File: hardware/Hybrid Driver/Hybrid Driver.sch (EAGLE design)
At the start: 35 parts, among them CN1 MTA100-6, CN2 SE14, U1 M57962L, U2 VLA106-15242, U3 M57962L, U4 VLA106-15242

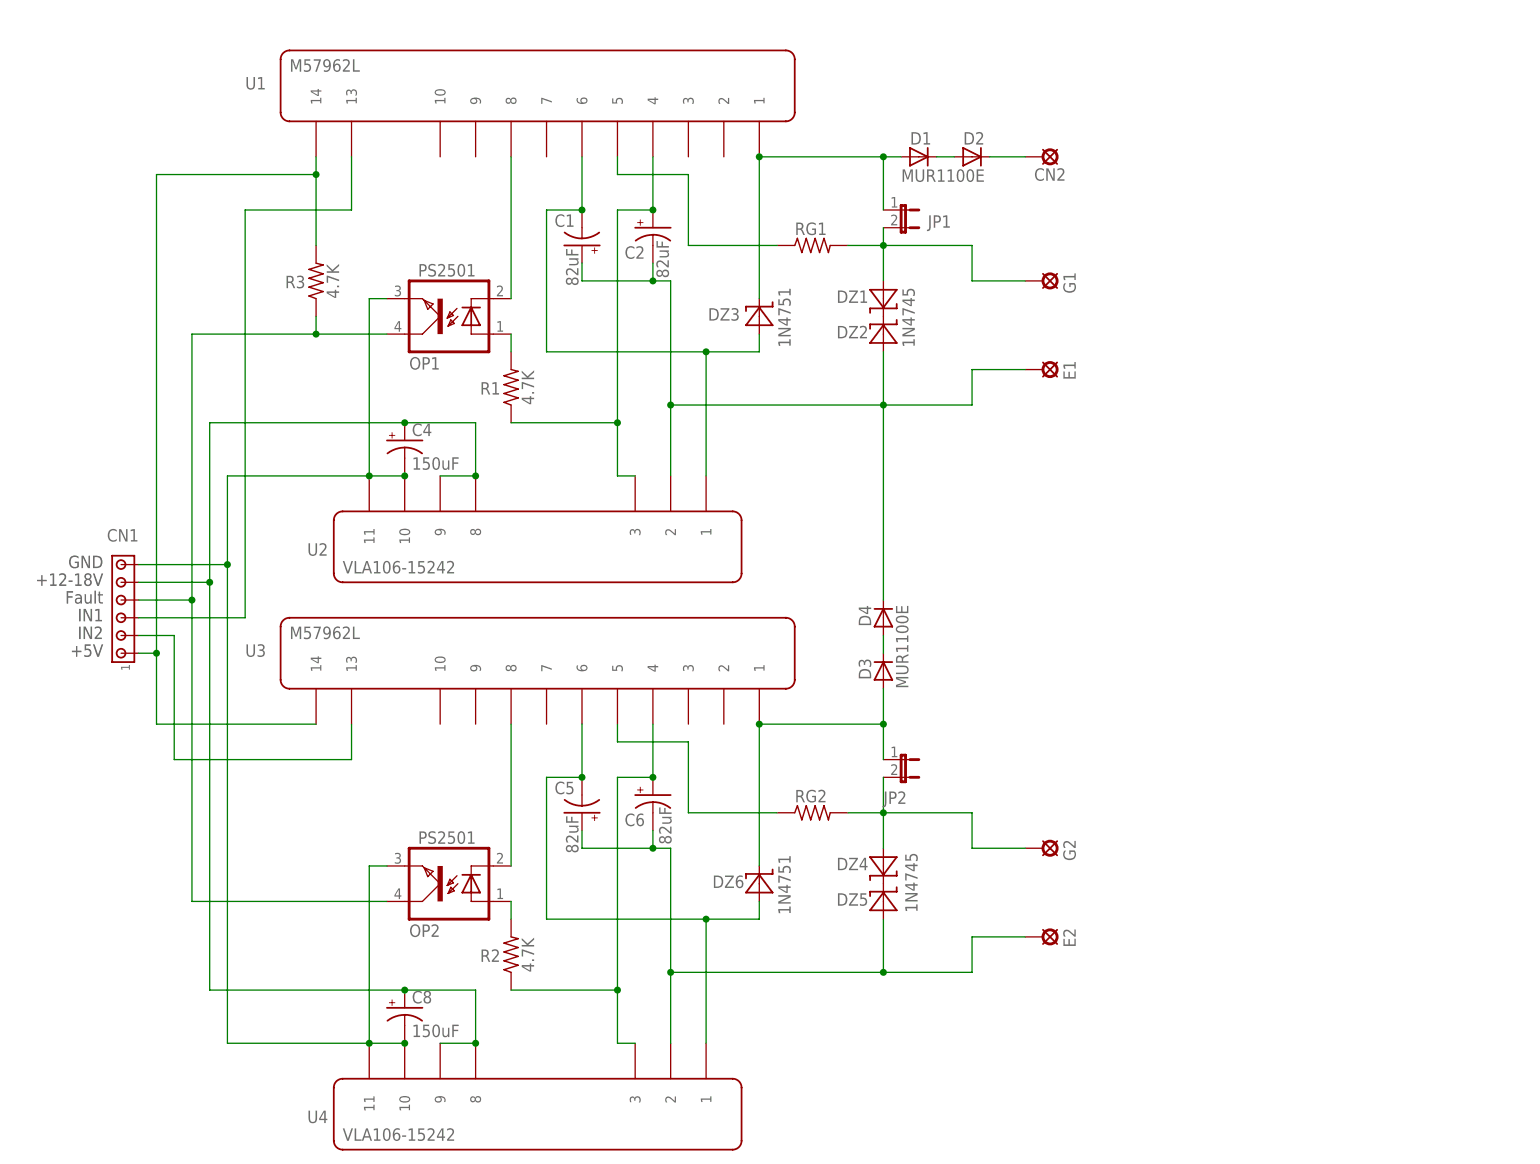
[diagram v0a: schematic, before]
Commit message: reduced board width to 2 inches, added decoupling cap on 5V supply, updated documentation and library components
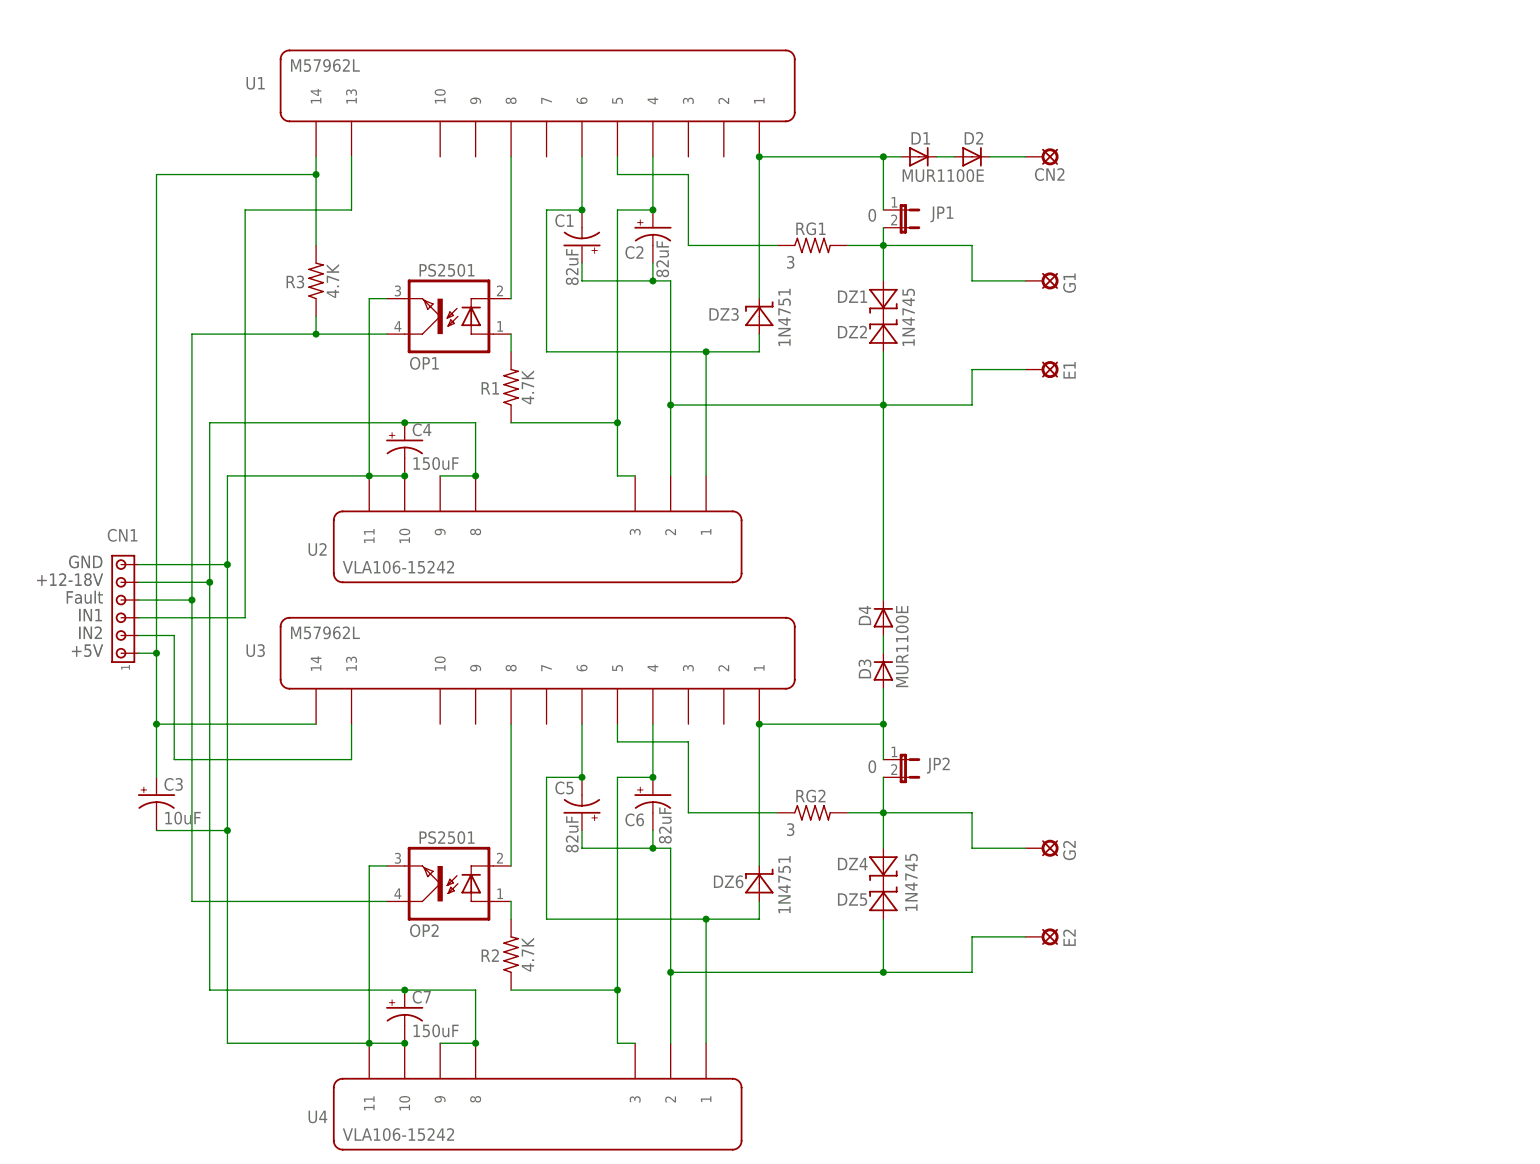
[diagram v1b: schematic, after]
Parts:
- added C3: 10uF, rcl:CPOL-USE2-5
- JP1, JP2: value (none) -> 0
- RG1, RG2: value (none) -> 3
- renumbered C8 to C7
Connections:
- net GND: now also C3.-
- net N$9: now also C3.+
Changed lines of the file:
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@@
 <?xml version="1.0" encoding="utf-8"?>
 <!DOCTYPE eagle SYSTEM "eagle.dtd">
-<eagle version="6.2">
+<eagle version="8.5.1">
 <drawing>
 <settings>
 <setting alwaysvectorfont="no"/>
+<setting keepoldvectorfont="yes"/>
 <setting verticaltext="up"/>
 </settings>
@@
 <part name="CN1" library="con-amp" deviceset="MTA06-100" device="" value="MTA100-6"/>
 <part name="U$2" library="1-Custom" deviceset="LETTER_L" device="">
+<attribute name="LICENSE" value="CC BY-SA"/>
 <attribute name="PROJECT" value="ReactorForge - Hybrid Driver"/>
-<attribute name="URL" value="https://github.com/joshcam/ReactorForge"/>
+<attribute name="URL" value="https://github.com/ThingEngineer/ReactorForge"/>
 </part>
 <part name="U4" library="1-Custom" deviceset="VLA106-15242" device=""/>
@@
 <part name="OP2" library="optocoupler" deviceset="PC817" device="" value="PS2501"/>
 <part name="C4" library="resistor" deviceset="CPOL-US" device="E5-8.5" value="150uF"/>
-<part name="C8" library="resistor" deviceset="CPOL-US" device="E5-8.5" value="150uF"/>
+<part name="C7" library="resistor" deviceset="CPOL-US" device="E5-8.5" value="150uF"/>
 <part name="C1" library="resistor" deviceset="CPOL-US" device="E2.5-7" value="82uF"/>
 <part name="C2" library="resistor" deviceset="CPOL-US" device="E2.5-7" value="82uF"/>
@@
 <part name="R2" library="resistor" deviceset="R-US_" device="0207/10" value="4.7K"/>
 <part name="R3" library="resistor" deviceset="R-US_" device="0207/10" value="4.7K"/>
-<part name="RG1" library="resistor" deviceset="R-US_" device="0309/12"/>
-<part name="RG2" library="resistor" deviceset="R-US_" device="0309/12"/>
+<part name="RG1" library="resistor" deviceset="R-US_" device="0309/12" value="3"/>
+<part name="RG2" library="resistor" deviceset="R-US_" device="0309/12" value="3"/>
 <part name="CN2" library="solpad" deviceset="SE14" device=""/>
 <part name="D1" library="diode" deviceset="OA95" device="" value="MUR1100E"/>
@@
 <part name="DZ3" library="1-Custom" deviceset="1N5338" device="" value="1N4751"/>
 <part name="DZ6" library="1-Custom" deviceset="1N5338" device="" value="1N4751"/>
-<part name="JP1" library="jumper" deviceset="JP1E" device=""/>
-<part name="JP2" library="jumper" deviceset="JP1E" device=""/>
+<part name="JP1" library="jumper" deviceset="JP1E" device="" value="0"/>
+<part name="JP2" library="jumper" deviceset="JP1E" device="" value="0"/>
 <part name="G1" library="1-Custom" deviceset="IGBT-PAD" device=""/>
 <part name="E1" library="1-Custom" deviceset="IGBT-PAD" device=""/>
 <part name="G2" library="1-Custom" deviceset="IGBT-PAD" device=""/>
 <part name="E2" library="1-Custom" deviceset="IGBT-PAD" device=""/>
+<part name="C3" library="rcl" library_urn="urn:adsk.eagle:library:334" deviceset="CPOL-US" device="E2-5" package3d_urn="urn:adsk.eagle:package:23346/2" value="10uF"/>
 </parts>
 <sheets>
@@
 <attribute name="VALUE" x="92.456" y="117.729" size="1.778" layer="96"/>
 </instance>
-<instance part="C8" gate="G$1" x="91.44" y="40.64" smashed="yes">
+<instance part="C7" gate="G$1" x="91.44" y="40.64" smashed="yes">
 <attribute name="NAME" x="92.456" y="41.275" size="1.778" layer="95"/>
 <attribute name="VALUE" x="92.456" y="36.449" size="1.778" layer="96"/>
@@
 </instance>
 <instance part="JP1" gate="A" x="162.56" y="154.94" smashed="yes" rot="R270">
-<attribute name="NAME" x="166.37" y="152.4" size="1.778" layer="95"/>
-<attribute name="VALUE" x="162.56" y="149.225" size="1.778" layer="96"/>
+<attribute name="NAME" x="166.878" y="153.67" size="1.778" layer="95"/>
+<attribute name="VALUE" x="157.734" y="153.289" size="1.778" layer="96"/>
 </instance>
 <instance part="JP2" gate="A" x="162.56" y="76.2" smashed="yes" rot="R270">
-<attribute name="NAME" x="160.02" y="69.85" size="1.778" layer="95"/>
-<attribute name="VALUE" x="162.56" y="70.485" size="1.778" layer="96"/>
+<attribute name="NAME" x="166.37" y="74.676" size="1.778" layer="95"/>
+<attribute name="VALUE" x="157.734" y="74.295" size="1.778" layer="96"/>
 </instance>
 <instance part="G1" gate="G$1" x="180.34" y="144.78" rot="R270"/>
@@
 <instance part="G2" gate="G$1" x="180.34" y="63.5" rot="R270"/>
 <instance part="E2" gate="G$1" x="180.34" y="50.8" rot="R270"/>
+<instance part="C3" gate="G$1" x="55.88" y="71.12"/>
 </instances>
 <busses>
@@
 <junction x="78.74" y="160.02"/>
 <wire x1="78.74" y1="160.02" x2="78.74" y2="162.56" width="0.1524" layer="91"/>
+<pinref part="C3" gate="G$1" pin="+"/>
+<wire x1="55.88" y1="73.66" x2="55.88" y2="81.28" width="0.1524" layer="91"/>
+<junction x="55.88" y="81.28"/>
 </segment>
 </net>
@@
 <wire x1="86.36" y1="60.96" x2="86.36" y2="35.56" width="0.1524" layer="91"/>
 <pinref part="U4" gate="G$1" pin="10"/>
-<pinref part="C8" gate="G$1" pin="-"/>
+<pinref part="C7" gate="G$1" pin="-"/>
 <junction x="91.44" y="35.56"/>
 <wire x1="91.44" y1="35.56" x2="86.36" y2="35.56" width="0.1524" layer="91"/>
@@
 <wire x1="66.04" y1="104.14" x2="66.04" y2="116.84" width="0.1524" layer="91"/>
 <wire x1="66.04" y1="116.84" x2="86.36" y2="116.84" width="0.1524" layer="91"/>
-<wire x1="66.04" y1="35.56" x2="66.04" y2="104.14" width="0.1524" layer="91"/>
+<wire x1="66.04" y1="35.56" x2="66.04" y2="66.04" width="0.1524" layer="91"/>
 <junction x="66.04" y="104.14"/>
+<pinref part="C3" gate="G$1" pin="-"/>
+<wire x1="66.04" y1="66.04" x2="66.04" y2="104.14" width="0.1524" layer="91"/>
+<wire x1="55.88" y1="66.04" x2="66.04" y2="66.04" width="0.1524" layer="91"/>
+<junction x="66.04" y="66.04"/>
 </segment>
 </net>
@@
 <wire x1="96.52" y1="35.56" x2="101.6" y2="35.56" width="0.1524" layer="91"/>
 <wire x1="101.6" y1="35.56" x2="101.6" y2="43.18" width="0.1524" layer="91"/>
-<pinref part="C8" gate="G$1" pin="+"/>
+<pinref part="C7" gate="G$1" pin="+"/>
 <junction x="91.44" y="43.18"/>
 <wire x1="101.6" y1="43.18" x2="91.44" y2="43.18" width="0.1524" layer="91"/>
@@
 </sheet>
 </sheets>
-<errors>
-</errors>
 </schematic>
 </drawing>
+<compatibility>
+<note version="8.2" severity="warning">
+Since Version 8.2, EAGLE supports online libraries. The ids
+of those online libraries will not be understood (or retained)
+with this version.
+</note>
+<note version="8.3" severity="warning">
+Since Version 8.3, EAGLE supports URNs for individual library
+assets (packages, symbols, and devices). The URNs of those assets
+will not be understood (or retained) with this version.
+</note>
+<note version="8.3" severity="warning">
+Since Version 8.3, EAGLE supports the association of 3D packages
+with devices in libraries, schematics, and board files. Those 3D
+packages will not be understood (or retained) with this version.
+</note>
+<note version="8.4" severity="warning">
+Since Version 8.4, EAGLE supports properties for SPICE simulation.
+Probes in schematics and SPICE mapping objects found in parts and library devices
+will not be understood with this version. Update EAGLE to the latest version
+for full support of SPICE simulation.
+</note>
+</compatibility>
 </eagle>

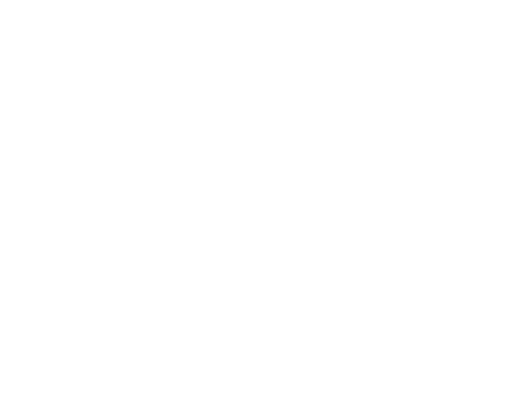
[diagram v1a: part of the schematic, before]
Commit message: added OSH logo, tweaked silkscreen
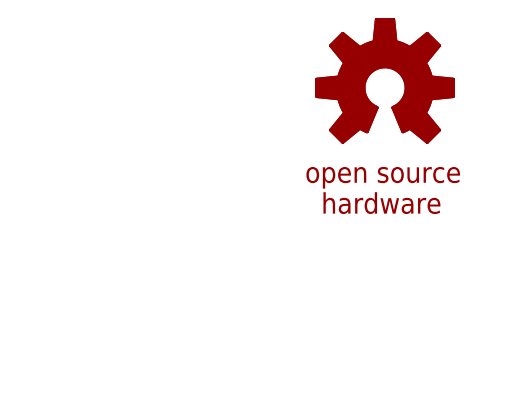
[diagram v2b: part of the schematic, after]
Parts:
- added GOLD_ORB_SM1: OSHWLOGOLOGO8MM, oshw:OSHWLOGOLOGO8MM
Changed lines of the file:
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@@
 <layer number="54" name="bGND_GNDA" color="7" fill="1" visible="no" active="no"/>
 <layer number="56" name="wert" color="7" fill="1" visible="no" active="no"/>
+<layer number="90" name="Modules" color="5" fill="1" visible="yes" active="yes"/>
 <layer number="91" name="Nets" color="2" fill="1" visible="yes" active="yes"/>
 <layer number="92" name="Busses" color="1" fill="1" visible="yes" active="yes"/>
@@
 <layer number="121" name="_tsilk" color="7" fill="1" visible="yes" active="yes"/>
 <layer number="122" name="_bsilk" color="7" fill="1" visible="yes" active="yes"/>
+<layer number="125" name="_tNames" color="7" fill="1" visible="yes" active="yes"/>
 <layer number="131" name="prix" color="7" fill="1" visible="yes" active="yes"/>
 <layer number="132" name="test" color="7" fill="1" visible="yes" active="yes"/>
+<layer number="144" name="Drill_legend" color="7" fill="1" visible="yes" active="yes"/>
 <layer number="151" name="HeatSink" color="7" fill="1" visible="yes" active="yes"/>
 <layer number="200" name="200bmp" color="7" fill="1" visible="yes" active="yes"/>
@@
 <layer number="207" name="207bmp" color="7" fill="1" visible="yes" active="yes"/>
 <layer number="208" name="208bmp" color="7" fill="1" visible="yes" active="yes"/>
+<layer number="209" name="209bmp" color="7" fill="1" visible="yes" active="yes"/>
+<layer number="210" name="210bmp" color="7" fill="1" visible="yes" active="yes"/>
+<layer number="211" name="211bmp" color="7" fill="1" visible="yes" active="yes"/>
+<layer number="212" name="212bmp" color="7" fill="1" visible="yes" active="yes"/>
+<layer number="213" name="213bmp" color="7" fill="1" visible="yes" active="yes"/>
+<layer number="214" name="214bmp" color="7" fill="1" visible="yes" active="yes"/>
+<layer number="215" name="215bmp" color="7" fill="1" visible="yes" active="yes"/>
+<layer number="216" name="216bmp" color="7" fill="1" visible="yes" active="yes"/>
 <layer number="250" name="Descript" color="7" fill="1" visible="yes" active="yes"/>
 <layer number="251" name="SMDround" color="7" fill="1" visible="yes" active="yes"/>
@@
 <part name="E2" library="1-Custom" deviceset="IGBT-PAD" device=""/>
 <part name="C3" library="rcl" library_urn="urn:adsk.eagle:library:334" deviceset="CPOL-US" device="E2-5" package3d_urn="urn:adsk.eagle:package:23346/2" value="10uF"/>
+<part name="GOLD_ORB_SM1" library="oshw" deviceset="OSHWLOGO" device="LOGO8MM"/>
 </parts>
 <sheets>
@@
 <instance part="E2" gate="G$1" x="180.34" y="50.8" rot="R270"/>
 <instance part="C3" gate="G$1" x="55.88" y="71.12"/>
+<instance part="GOLD_ORB_SM1" gate="G$1" x="238.76" y="175.26"/>
 </instances>
 <busses>
@@
 </drawing>
 <compatibility>
+<note version="6.3" minversion="6.2.2" severity="warning">
+Since Version 6.2.2 text objects can contain more than one line,
+which will not be processed correctly with this version.
+</note>
 <note version="8.2" severity="warning">
 Since Version 8.2, EAGLE supports online libraries. The ids
